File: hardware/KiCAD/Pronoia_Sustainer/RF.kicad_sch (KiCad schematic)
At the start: 10 parts, among them J12 132203, J13 Conn_01x04_Socket, J14 ANTENNA_PAD, U7 NEO-M9N, U8 RFM95W-915S2

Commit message: updated Schematics
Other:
- note added: "Antenna (Rubber Ducky, or fabricate 1/4 wave or 1/2 wave)"
- note removed: "1/4 wave Wire Whip Antenna"
- moved on the sheet: J14
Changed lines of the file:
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@@
 	(text "Parts Not Shown"
 		(exclude_from_sim no)
-		(at 253.238 19.558 0)
+		(at 237.744 19.812 0)
 		(effects
 			(font
@@
 		)
 	)
-	(text "1/4 wave Wire Whip Antenna"
+	(text "Antenna (Rubber Ducky, or fabricate 1/4 wave or 1/2 wave)"
 		(exclude_from_sim no)
-		(at 250.952 27.178 0)
+		(at 251.714 25.4 0)
 		(effects
 			(font
@@
 	(wire
 		(pts
-			(xy 161.29 87.63) (xy 163.83 87.63)
+			(xy 161.29 87.63) (xy 167.64 87.63)
 		)
 		(stroke
@@
 	(symbol
 		(lib_id "Connector_Generic:Conn_01x01")
-		(at 168.91 87.63 0)
+		(at 172.72 87.63 0)
 		(unit 1)
 		(exclude_from_sim no)
@@
 		(fields_autoplaced yes)
 		(property "Reference" "J14"
-			(at 171.45 86.3599 0)
+			(at 175.26 86.3599 0)
 			(effects
 				(font
@@
 		)
 		(property "Value" "ANTENNA_PAD"
-			(at 171.45 88.8999 0)
+			(at 175.26 88.8999 0)
 			(effects
 				(font
@@
 		)
 		(property "Footprint" "Connector_PinHeader_2.54mm:PinHeader_1x01_P2.54mm_Vertical"
-			(at 168.91 87.63 0)
+			(at 172.72 87.63 0)
 			(effects
 				(font
@@
 		)
 		(property "Datasheet" "~"
-			(at 168.91 87.63 0)
+			(at 172.72 87.63 0)
 			(effects
 				(font
@@
 		)
 		(property "Description" "Generic connector, single row, 01x01, script generated (kicad-library-utils/schlib/autogen/connector/)"
-			(at 168.91 87.63 0)
+			(at 172.72 87.63 0)
 			(effects
 				(font
@@
 		)
 		(property "LCSC" ""
-			(at 168.91 87.63 0)
-			(effects
-				(font
+			(at 172.72 87.63 0)
+			(effects
+				(font

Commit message: Completed 1st draft of Schematic
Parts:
- removed BT1: MS621FE-FL11E, MS621FE-FL11E:BAT_MS621FE-FL11E, symbol MS621FE-FL11E:MS621FE-FL11E
- removed D7: BAT54, PCM_JLCPCB:D_SOT-23, symbol PCM_JLCPCB-Diodes:Schottky,BAT54
- removed R29: 680Ω, PCM_JLCPCB:R_0402, symbol PCM_JLCPCB-Resistors:0402,680Ω
- added BT2: MS621FE-FL11E, MS621FE-FL11E:BAT_MS621FE-FL11E, symbol MS621FE-FL11E:MS621FE-FL11E
- added D5: BAT54, PCM_JLCPCB:D_SOT-23, symbol PCM_JLCPCB-Diodes:Schottky,BAT54
- added R19: 680Ω, PCM_JLCPCB:R_0402, symbol PCM_JLCPCB-Resistors:0402,680Ω
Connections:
- net +3.3V: now also D5.1
- net GND: now also BT2.-
- net at U7.22 (V_BCKP): now also BT2.+, R19.1
- new net: D5.3, R19.2
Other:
- note added: "3V Battery Charging Circuit"
- note added: "Bias Tee Circuit"
- note added: "Bluetooth Breakout Module Connects via Headers"
- note added: "GPS 3V Backup Battery"
- note added: "Monopole or Dipole Antenna 1/4 wavelength=3.23 in"
- note added: "SMA Female Socket Connects to Patch Antenna"
- note removed: "Bluetooth Breakout Module"
- moved on the sheet: C15, J12, J13, J14, L2, U7, U8

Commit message: Last commit for KiCAD schematic w/ GPS, Telem, and Bluetooth
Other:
- company: (none) -> Walla Walla University
- title: (none) -> Pronoia Sustainer Communications
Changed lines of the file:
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@@
 	(generator_version "9.0")
 	(paper "A4")
+	(title_block
+		(title "Pronoia Sustainer Communications")
+		(date "2026-02-03")
+		(rev "1.0")
+		(company "Walla Walla University")
+		(comment 1 "Prometheus Rocket Project")
+	)
 	(text "Bluetooth Breakout Module\nConnects via Headers"
 		(exclude_from_sim no)

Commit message: Finalized v2.0 of Pronoia Schematic
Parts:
- removed BT2: MS621FE-FL11E, MS621FE-FL11E:BAT_MS621FE-FL11E, symbol MS621FE-FL11E:MS621FE-FL11E
- removed C15: 100pF, PCM_JLCPCB:C_0805, symbol PCM_JLCPCB-Capacitors:0805,100pF
- removed D5: BAT54, PCM_JLCPCB:D_SOT-23, symbol PCM_JLCPCB-Diodes:Schottky,BAT54
- removed J12: 132203, Connector_Coaxial:SMA_Amphenol_132203-12_Horizontal, symbol 132203:132203
- removed J13: Conn_01x04_Socket, Connector_PinSocket_2.54mm:PinSocket_1x04_P2.54mm_Vertical, symbol Connector:Conn_01x04_Socket
- removed J14: ANTENNA_PAD, Connector_PinHeader_2.54mm:PinHeader_1x01_P2.54mm_Vertical, symbol Connector_Generic:Conn_01x01
- removed L2: 33nH, Inductor_SMD:L_0402_1005Metric, symbol Device:L
- removed R19: 680Ω, PCM_JLCPCB:R_0402, symbol PCM_JLCPCB-Resistors:0402,680Ω
- removed U7: NEO-M9N, RF_GPS:ublox_NEO, symbol RF_GPS:NEO-M9N
- removed U8: RFM95W-915S2, RF_Module:HOPERF_RFM9XW_SMD, symbol RF_Module:RFM95W-915S2
- added J8: 640457-4, 640457-4:TE_640457-4, symbol 640457-4:640457-4
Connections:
- net GND: now also J8.2
- new net GX-12-4_Detect: J8.1
- new net GX-12-4_RX: J8.4
- new net GX-12-4_TX: J8.3
- no-connect marks 15 -> 0
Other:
- note added: "GX-12 Connection for Pre-Flight Protocol Connects via Locked Headers"
- note added: "GX-12 Male Connected to 1x4 Locked Header"
- note removed: "3V Battery Charging Circuit"
- note removed: "Antenna (Rubber Ducky, or fabricate 1/4 wave or 1/2 wave)"
- note removed: "Bias Tee Circuit"
- note removed: "Bluetooth Breakout Module Connects via Headers"
- note removed: "GPS 3V Backup Battery"
- note removed: "GPS Module"
- note removed: "Monopole or Dipole Antenna 1/4 wavelength=3.23 in"
- note removed: "SMA Female Socket Connects to Patch Antenna"
- note removed: "Telemetry"

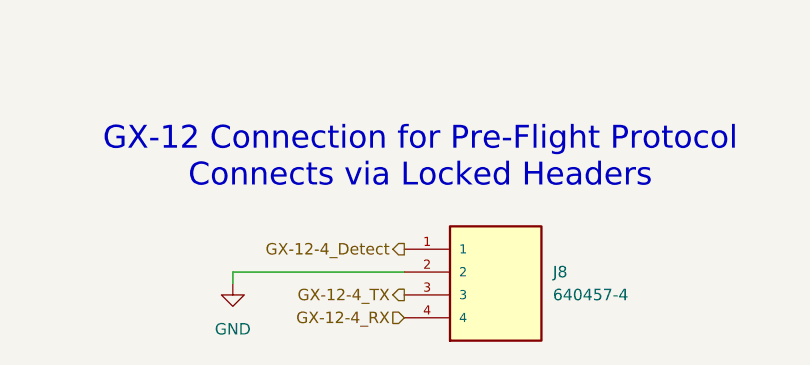
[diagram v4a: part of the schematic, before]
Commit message: Finished PCB layout
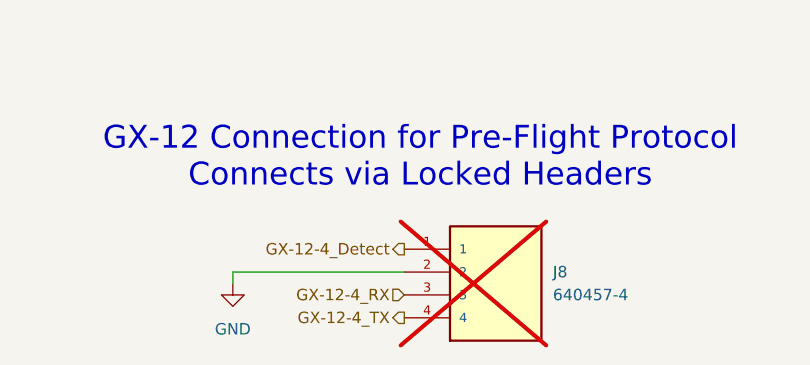
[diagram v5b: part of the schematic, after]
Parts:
- J8: now not fitted
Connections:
- net GX-12-4_RX: now also J8.3; no longer J8.4
- net GX-12-4_TX: now also J8.4; no longer J8.3
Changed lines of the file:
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@@
 	(hierarchical_label "GX-12-4_RX"
 		(shape input)
-		(at 175.26 119.38 180)
+		(at 175.26 116.84 180)
 		(effects
 			(font
@@
 	(hierarchical_label "GX-12-4_TX"
 		(shape output)
-		(at 175.26 116.84 180)
+		(at 175.26 119.38 180)
 		(effects
 			(font
@@
 		(in_bom yes)
 		(on_board yes)
-		(dnp no)
+		(dnp yes)
 		(fields_autoplaced yes)
 		(property "Reference" "J8"
@@
 			)
 		)
+		(property "LCSC" ""
+			(at 185.42 116.84 0)
+			(effects
+				(font
+					(size 1.27 1.27)
+				)
+			)
+		)

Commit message: Sensor Bring-Up
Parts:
- J8: now left out of the parts list
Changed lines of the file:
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@@
 (kicad_sch
-	(version 20250114)
+	(version 20260306)
 	(generator "eeschema")
-	(generator_version "9.0")
+	(generator_version "10.0")
 	(paper "A4")
 	(title_block
@@
 		(at 185.42 116.84 0)
 		(unit 1)
+		(body_style 1)
 		(exclude_from_sim no)
-		(in_bom yes)
+		(in_bom no)
 		(on_board yes)
+		(in_pos_files yes)
 		(dnp yes)
 		(fields_autoplaced yes)
 		(property "Reference" "J8"
 			(at 191.77 114.2999 0)
+			(show_name no)
+			(do_not_autoplace no)
 			(effects
 				(font
@@
 		(property "Value" "640457-4"
 			(at 191.77 116.8399 0)
+			(show_name no)
+			(do_not_autoplace no)
 			(effects
 				(font
@@
 		(property "Footprint" "640457-4:TE_640457-4"
 			(at 185.42 116.84 0)
-			(effects
-				(font
-					(size 1.27 1.27)
-				)
-				(justify bottom)
-				(hide yes)
+			(hide yes)
+			(show_name no)
+			(do_not_autoplace no)
+			(effects
+				(font
+					(size 1.27 1.27)
+				)
+				(justify bottom)
 			)
 		)
 		(property "Datasheet" ""
 			(at 185.42 116.84 0)
-			(effects
-				(font
-					(size 1.27 1.27)
-				)
-				(hide yes)
+			(hide yes)
+			(show_name no)
+			(do_not_autoplace no)
+			(effects
+				(font
+					(size 1.27 1.27)
+				)
 			)
 		)
 		(property "Description" ""
 			(at 185.42 116.84 0)
-			(effects
-				(font
-					(size 1.27 1.27)
-				)
-				(hide yes)
+			(hide yes)
+			(show_name no)
+			(do_not_autoplace no)
+			(effects
+				(font
+					(size 1.27 1.27)
+				)
 			)
 		)
 		(property "Comment" "640457-4"
 			(at 185.42 116.84 0)
-			(effects
-				(font
-					(size 1.27 1.27)
-				)
-				(justify bottom)
-				(hide yes)
+			(hide yes)
+			(show_name no)
+			(do_not_autoplace no)
+			(effects
+				(font
+					(size 1.27 1.27)
+				)
+				(justify bottom)
 			)
 		)
 		(property "MF" "TE Connectivity"
 			(at 185.42 116.84 0)
-			(effects
-				(font
-					(size 1.27 1.27)
-				)
-				(justify bottom)
-				(hide yes)
+			(hide yes)
+			(show_name no)
+			(do_not_autoplace no)
+			(effects
+				(font
+					(size 1.27 1.27)
+				)
+				(justify bottom)
 			)
 		)
 		(property "Description_1" "Header 0.1 in. (Centerline) White (Housing) Polyester 4 UL 94V-0 | TE Connectivity 640457-4"
 			(at 185.42 116.84 0)
-			(effects
-				(font
-					(size 1.27 1.27)
-				)
-				(justify bottom)
-				(hide yes)
+			(hide yes)
+			(show_name no)
+			(do_not_autoplace no)
+			(effects
+				(font
+					(size 1.27 1.27)
+				)
+				(justify bottom)
 			)
 		)
 		(property "Package" "None"
 			(at 185.42 116.84 0)
-			(effects
-				(font
-					(size 1.27 1.27)
-				)
-				(justify bottom)
-				(hide yes)
+			(hide yes)
+			(show_name no)
+			(do_not_autoplace no)
+			(effects
+				(font
+					(size 1.27 1.27)
+				)
+				(justify bottom)
 			)
 		)
 		(property "Price" "None"
 			(at 185.42 116.84 0)
-			(effects
-				(font
-					(size 1.27 1.27)
-				)
-				(justify bottom)
-				(hide yes)
+			(hide yes)
+			(show_name no)
+			(do_not_autoplace no)
+			(effects
+				(font
+					(size 1.27 1.27)
+				)
+				(justify bottom)
 			)
 		)
 		(property "Check_prices" "https://www.snapeda.com/parts/640457-4/TE+Connectivity+AMP+Connectors/view-part/?ref=eda"
 			(at 185.42 116.84 0)
-			(effects
-				(font
-					(size 1.27 1.27)
-				)
-				(justify bottom)
-				(hide yes)
+			(hide yes)
+			(show_name no)
+			(do_not_autoplace no)
+			(effects
+				(font
+					(size 1.27 1.27)
+				)
+				(justify bottom)
 			)
 		)
 		(property "STANDARD" "Manufacturer Recommendations"
 			(at 185.42 116.84 0)
-			(effects
-				(font
-					(size 1.27 1.27)
-				)
-				(justify bottom)
-				(hide yes)
+			(hide yes)
+			(show_name no)
+			(do_not_autoplace no)
+			(effects
+				(font
+					(size 1.27 1.27)
+				)
+				(justify bottom)
 			)
 		)
 		(property "PARTREV" "R"
 			(at 185.42 116.84 0)
-			(effects
-				(font
-					(size 1.27 1.27)
-				)
-				(justify bottom)
-				(hide yes)
+			(hide yes)
+			(show_name no)
+			(do_not_autoplace no)
+			(effects
+				(font
+					(size 1.27 1.27)
+				)
+				(justify bottom)
 			)
 		)
 		(property "SnapEDA_Link" "https://www.snapeda.com/parts/640457-4/TE+Connectivity+AMP+Connectors/view-part/?ref=snap"
 			(at 185.42 116.84 0)
-			(effects
-				(font
-					(size 1.27 1.27)
-				)
-				(justify bottom)
-				(hide yes)
+			(hide yes)
+			(show_name no)
+			(do_not_autoplace no)
+			(effects
+				(font
+					(size 1.27 1.27)
+				)
+				(justify bottom)
 			)
 		)
 		(property "MP" "640457-4"
 			(at 185.42 116.84 0)
-			(effects
-				(font
-					(size 1.27 1.27)
-				)
-				(justify bottom)
-				(hide yes)
+			(hide yes)
+			(show_name no)
+			(do_not_autoplace no)
+			(effects
+				(font
+					(size 1.27 1.27)
+				)
+				(justify bottom)
 			)
 		)
 		(property "Purchase-URL" "https://www.snapeda.com/api/url_track_click_mouser/?unipart_id=390414&manufacturer=TE Connectivity&part_name=640457-4&search_term=None"
 			(at 185.42 116.84 0)
-			(effects
-				(font
-					(size 1.27 1.27)
-				)
-				(justify bottom)
-				(hide yes)
+			(hide yes)
+			(show_name no)
+			(do_not_autoplace no)
+			(effects
+				(font
+					(size 1.27 1.27)
+				)
+				(justify bottom)
 			)
 		)
 		(property "Availability" "In Stock"
 			(at 185.42 116.84 0)
-			(effects
-				(font
-					(size 1.27 1.27)
-				)
-				(justify bottom)
-				(hide yes)
+			(hide yes)
+			(show_name no)
+			(do_not_autoplace no)
+			(effects
+				(font
+					(size 1.27 1.27)
+				)
+				(justify bottom)
 			)
 		)
 		(property "MANUFACTURER" "TE"
 			(at 185.42 116.84 0)
-			(effects
-				(font
-					(size 1.27 1.27)
-				)
-				(justify bottom)
-				(hide yes)
+			(hide yes)
+			(show_name no)
+			(do_not_autoplace no)
+			(effects
+				(font
+					(size 1.27 1.27)
+				)
+				(justify bottom)
 			)
 		)
 		(property "LCSC" ""
 			(at 185.42 116.84 0)
+			(show_name no)
+			(do_not_autoplace no)
+			(effects
+				(font
+					(size 1.27 1.27)
+				)
+			)
+		)
+		(property "LCSC Part" ""
+			(at 185.42 116.84 0)
+			(hide yes)
+			(show_name no)
+			(do_not_autoplace no)
 			(effects
 				(font
@@
 		)
 		(instances
-			(project ""
+			(project "Pronoia_Sustainer"
 				(path "/33e0e590-80be-4096-a732-129afca197c6/a319d727-a504-4e2a-8ae8-c5d7a33202ff"
 					(reference "J8")
@@
 		(at 156.21 115.57 0)
 		(unit 1)
+		(body_style 1)
 		(exclude_from_sim no)
 		(in_bom yes)
 		(on_board yes)
+		(in_pos_files yes)
 		(dnp no)
 		(fields_autoplaced yes)
 		(property "Reference" "#PWR03"
 			(at 156.21 121.92 0)
-			(effects
-				(font
-					(size 1.27 1.27)
-				)
-				(hide yes)
+			(hide yes)
+			(show_name no)
+			(do_not_autoplace no)
+			(effects
+				(font
+					(size 1.27 1.27)
+				)
 			)
 		)
 		(property "Value" "GND"
 			(at 156.21 120.65 0)
+			(show_name no)
+			(do_not_autoplace no)
 			(effects
 				(font
@@
 		(property "Footprint" ""
 			(at 156.21 115.57 0)
-			(effects
-				(font
-					(size 1.27 1.27)
-				)
-				(hide yes)
+			(hide yes)
+			(show_name no)
+			(do_not_autoplace no)
+			(effects
+				(font
+					(size 1.27 1.27)
+				)
 			)
 		)
 		(property "Datasheet" ""
 			(at 156.21 115.57 0)
-			(effects
-				(font
-					(size 1.27 1.27)
-				)
-				(hide yes)
+			(hide yes)
+			(show_name no)
+			(do_not_autoplace no)
+			(effects
+				(font
+					(size 1.27 1.27)
+				)
 			)
 		)
 		(property "Description" "Power symbol creates a global label with name \"GND\" , ground"
 			(at 156.21 115.57 0)
-			(effects
-				(font
-					(size 1.27 1.27)
-				)
-				(hide yes)
-			)
-		)
+			(hide yes)
+			(show_name no)
+			(do_not_autoplace no)
+			(effects
+				(font
+					(size 1.27 1.27)
+				)
+			)
+		)
